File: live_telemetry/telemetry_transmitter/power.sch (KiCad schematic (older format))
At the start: 36 parts, among them J2 Battery In, J3 BUS_CONN, Q1 Q_NMOS_GSD, Q2 Q_NMOS_GSD, Q3 Q_PMOS_GSD, Q4 Q_PMOS_GSD, Q5 Q_NMOS_GSD, U3 AP2114H-3.3, U5 INA180, U6 AP1509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

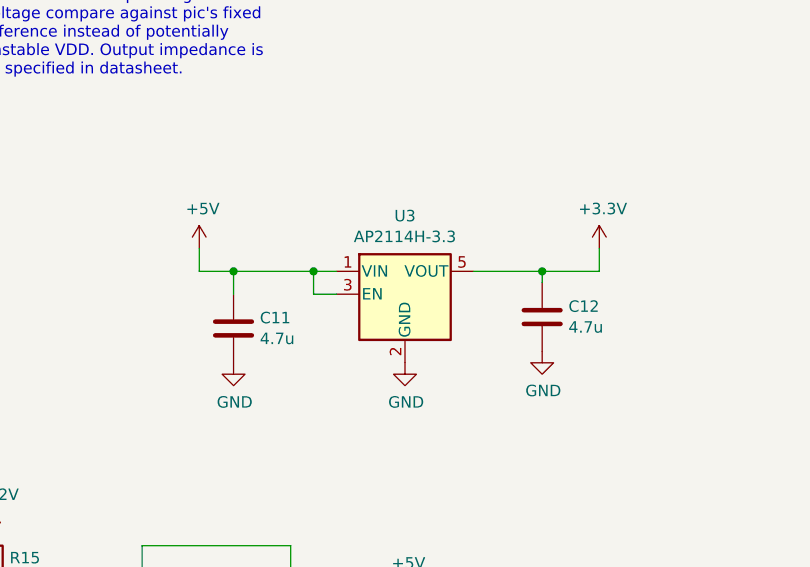
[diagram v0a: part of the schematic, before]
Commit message: Remove old/replaced components for LTT and LTR
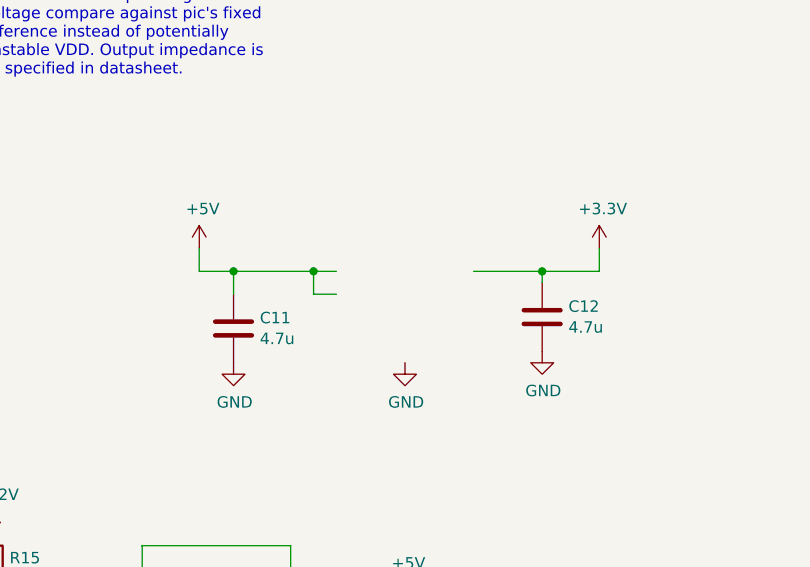
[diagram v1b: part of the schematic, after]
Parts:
- removed U3: AP2114H-3.3, Package_TO_SOT_SMD:SOT-23-5_HandSoldering, symbol Regulator_Linear:AP2112K-3.3
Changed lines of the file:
@@
 EESchema Schematic File Version 4
-EELAYER 26 0
+LIBS:telemetry_transmitter-cache
+EELAYER 29 0
 EELAYER END
 $Descr A4 11693 8268
@@
 	5000 1050 5000 1100
 $Comp
-L Regulator_Linear:AP2112K-3.3 U3
-U 1 1 5B9DEFF0
-P 9150 2600
-F 0 "U3" H 9150 2942 50  0000 C CNN
-F 1 "AP2114H-3.3" H 9150 2851 50  0000 C CNN
-F 2 "Package_TO_SOT_SMD:SOT-23-5_HandSoldering" H 9150 2925 50  0001 C CNN
-F 3 "https://www.diodes.com/assets/Datasheets/AP2112.pdf" H 9150 2700 50  0001 C CNN
-	1    9150 2600
-	1    0    0    -1
-$EndComp
-$Comp
 L Device:D_Zener D4

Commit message: Add placeholder LDOs for LTT and LTR
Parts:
- added U?: ?, Package_TO_SOT_SMD:TSOT-23-5, symbol Regulator_Linear:NCV8114ASN330T1G
- C11, C12: value 4.7u -> 1uF
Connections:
- wire segments 111 -> 112
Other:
- note added: "5V to 3.3V VOLTAGE REGULATOR"
- note added: "Note: The actual voltage regulator part # has not been selected yet. TBD ASAP."
- moved on the sheet: C11
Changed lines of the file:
@@
 L Device:C C11
 U 1 1 5B9E51A5
-P 8400 2750
-F 0 "C11" H 8285 2704 50  0000 R CNN
-F 1 "4.7u" H 8285 2795 50  0000 R CNN
-F 2 "Capacitor_SMD:C_0805_2012Metric_Pad1.15x1.40mm_HandSolder" H 8438 2600 50  0001 C CNN
-F 3 "~" H 8400 2750 50  0001 C CNN
-	1    8400 2750
+P 8350 2750
+F 0 "C11" H 8235 2704 50  0000 R CNN
+F 1 "1uF" H 8235 2795 50  0000 R CNN
+F 2 "Capacitor_SMD:C_0805_2012Metric_Pad1.15x1.40mm_HandSolder" H 8388 2600 50  0001 C CNN
+F 3 "~" H 8350 2750 50  0001 C CNN
+	1    8350 2750
 	-1   0    0    1
 $EndComp
@@
 P 9750 2700
 F 0 "C12" H 9635 2654 50  0000 R CNN
-F 1 "4.7u" H 9635 2745 50  0000 R CNN
+F 1 "1uF" H 9635 2745 50  0000 R CNN
 F 2 "Capacitor_SMD:C_0805_2012Metric_Pad1.15x1.40mm_HandSolder" H 9788 2550 50  0001 C CNN
 F 3 "~" H 9750 2700 50  0001 C CNN
@@
 $EndComp
 Wire Wire Line
-	9450 2500 9750 2500
-Wire Wire Line
 	9750 2500 9750 2550
 Wire Wire Line
-	8400 2500 8400 2600
-Wire Wire Line
-	8850 2600 8750 2600
+	8350 2500 8350 2600
 $Comp
 L power:+5V #PWR042
@@
 L power:GND #PWR043
 U 1 1 5B9E6978
-P 8400 2900
-F 0 "#PWR043" H 8400 2650 50  0001 C CNN
-F 1 "GND" H 8405 2727 50  0000 C CNN
-F 2 "" H 8400 2900 50  0001 C CNN
-F 3 "" H 8400 2900 50  0001 C CNN
-	1    8400 2900
+P 8350 2900
+F 0 "#PWR043" H 8350 2650 50  0001 C CNN
+F 1 "GND" H 8355 2727 50  0000 C CNN
+F 2 "" H 8350 2900 50  0001 C CNN
+F 3 "" H 8350 2900 50  0001 C CNN
+	1    8350 2900
 	1    0    0    -1
 $EndComp
@@
 	10000 2400 10000 2500
 Wire Wire Line
-	8750 2600 8750 2500
-Wire Wire Line
-	8400 2500 8750 2500
-Connection ~ 8750 2500
-Wire Wire Line
-	8750 2500 8850 2500
-Wire Wire Line
 	8250 2400 8250 2500
 Wire Wire Line
-	8250 2500 8400 2500
-Connection ~ 8400 2500
+	8250 2500 8350 2500
 Text GLabel 9450 5100 0    50   Input ~ 0
 CANH
@@
 	1    0    0    -1
 $EndComp
+Wire Wire Line
+	9550 2500 9750 2500
+Wire Wire Line
+	9450 2500 9550 2500
+Connection ~ 9550 2500
+$Comp
+L Regulator_Linear:NCV8114ASN330T1G U?
+U 1 1 61536AE4
+P 9150 2600
+F 0 "U?" H 9150 2967 50  0000 C CNN
+F 1 "?" H 9150 2876 50  0000 C CNN
+F 2 "Package_TO_SOT_SMD:TSOT-23-5" H 9150 2200 50  0001 C CIN
+F 3 "https://ru.mouser.com/datasheet/2/308/NCV8114-D-1107616.pdf" H 9150 2100 50  0001 C CNN
+	1    9150 2600
+	1    0    0    -1
+$EndComp
+Wire Wire Line
+	8750 2700 8650 2700
+Wire Wire Line
+	8650 2700 8650 2500
+Connection ~ 8650 2500
+Wire Wire Line
+	8650 2500 8750 2500
+Connection ~ 8350 2500
+Wire Wire Line
+	8350 2500 8650 2500
+Wire Notes Line
+	8050 2150 8050 3300
+Wire Notes Line
+	8050 3300 10200 3300
+Wire Notes Line
+	10200 3300 10200 2150
+Wire Notes Line
+	10200 2150 8050 2150
+Text Notes 8550 3250 0    50   ~ 10
+5V to 3.3V VOLTAGE REGULATOR
+Text Notes 7700 2100 0    50   ~ 10
+Note: The actual voltage regulator part # has not been selected yet. TBD ASAP.
 $EndSCHEMATC

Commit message: Add back LTR power.sch with battery connection, label symbols
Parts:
- gave numbers to parts that had none: 1
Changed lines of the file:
@@
 Connection ~ 9550 2500
 $Comp
-L Regulator_Linear:NCV8114ASN330T1G U?
+L Regulator_Linear:NCV8114ASN330T1G U3
 U 1 1 61536AE4
 P 9150 2600
-F 0 "U?" H 9150 2967 50  0000 C CNN
+F 0 "U3" H 9150 2967 50  0000 C CNN
 F 1 "?" H 9150 2876 50  0000 C CNN
 F 2 "Package_TO_SOT_SMD:TSOT-23-5" H 9150 2200 50  0001 C CIN

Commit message: Address PR comments and add in missing part #'s
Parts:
- removed U3: ?, Package_TO_SOT_SMD:TSOT-23-5, symbol Regulator_Linear:NCV8114ASN330T1G
- added U?: TLV70233QDBVRQ1, symbol canhw:TLV70233QDBVRQ1
- D4: value Schottky Diode -> SD1206S040S2R0
- F1: value Fuse -> F4989-ND, 36-3557-2-ND
- R10: value R -> 5K
- R11: value R -> 20K
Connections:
- wire segments 112 -> 120
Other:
- note added: "0.2R with \n1/4 W rating"
- note added: "12V to 5V BUCK CONVERTER"
- note added: "BATT VSENSE VOLTAGE DIVIDER"
- note added: "BATTERY CONNECTOR AND CURRENT SENSING"
- note added: "BUS CURRENT SENSING"
- note added: "CAN BUS CONNECTOR"
- note added: "Overspec'd Fuse\nof 58 V, 10A\n(Fuse & Holder)"
- moved on the sheet: C10, C11, C12, C5, C6, C7, C8, C9, D4, F1, J2, J3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

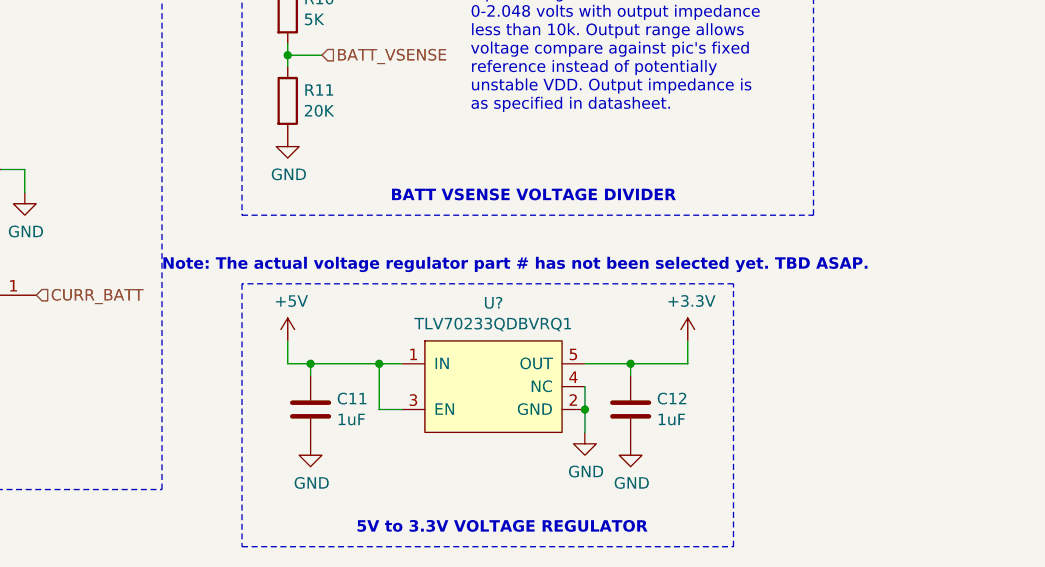
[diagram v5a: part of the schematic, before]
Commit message: Update radio schematics and set foot print associations
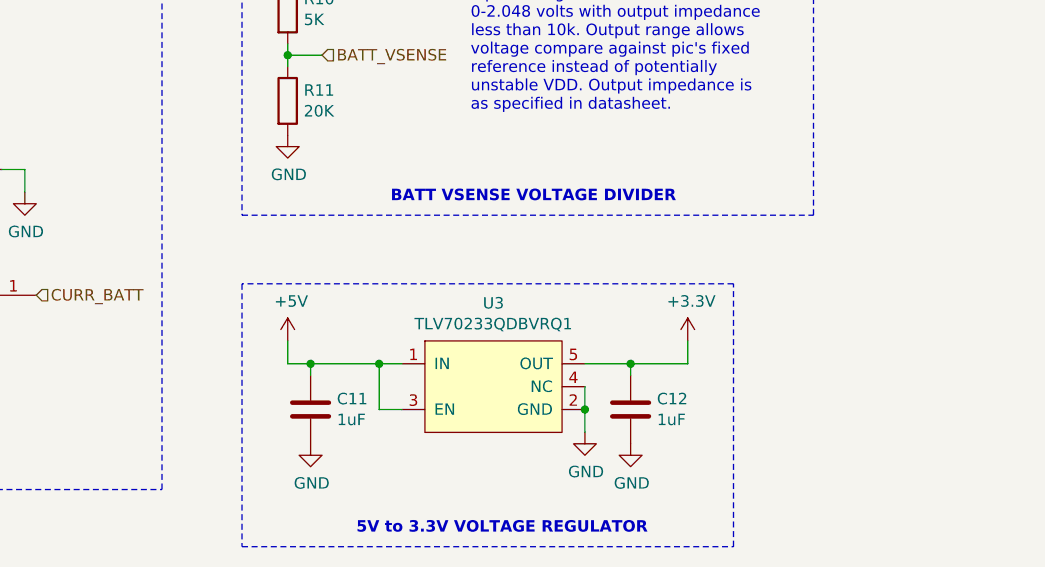
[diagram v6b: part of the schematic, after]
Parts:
- U3: renamed from U?; footprint (none) -> Package_TO_SOT_SMD:SOT-23-5_HandSoldering
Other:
- note removed: "Note: The actual voltage regulator part # has not been selected yet. TBD ASAP."
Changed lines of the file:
@@
 Text Notes 9000 3400 0    50   ~ 10
 5V to 3.3V VOLTAGE REGULATOR
-Text Notes 8150 2250 0    50   ~ 10
-Note: The actual voltage regulator part # has not been selected yet. TBD ASAP.
 Text Notes 6250 1100 0    50   ~ 0
 0.2R with \n1/4 W rating
@@
 	5800 1100 5800 1400
 $Comp
-L canhw:TLV70233QDBVRQ1 U?
+L canhw:TLV70233QDBVRQ1 U3
 U 1 1 615CA06D
 P 9600 3000
-F 0 "U?" H 9600 3615 50  0000 C CNN
+F 0 "U3" H 9600 3615 50  0000 C CNN
 F 1 "TLV70233QDBVRQ1" H 9600 3524 50  0000 C CNN
-F 2 "" H 9600 2950 50  0001 C CNN
+F 2 "Package_TO_SOT_SMD:SOT-23-5_HandSoldering" H 9600 2950 50  0001 C CNN
 F 3 "" H 9600 2950 50  0001 C CNN
 	1    9600 3000

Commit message: Update LTT first pass layout
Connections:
- net +12V: now also C5.1; no longer C5.2
- net +5V: now also C9.1; no longer C9.2
- net GND: now also C5.2, C9.2; no longer C5.1, C9.1
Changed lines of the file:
@@
-$EndComp
-$Comp
-L Device:C C9
-U 1 1 5B9E08AC
-P 3000 3250
-F 0 "C9" H 2885 3204 50  0000 R CNN
-F 1 "100u" H 2885 3295 50  0000 R CNN
-F 2 "Capacitor_THT:CP_Radial_D7.5mm_P2.50mm" H 3038 3100 50  0001 C CNN
-F 3 "~" H 3000 3250 50  0001 C CNN
-	1    3000 3250
-	-1   0    0    1
 $EndComp
 $Comp
@@
 	2250 3000 2500 3000
 Wire Wire Line
-	3000 3100 3000 3000
-Wire Wire Line
 	3000 3000 2800 3000
 $Comp
@@
 U 1 1 5BB56714
 P 2050 1350
-F 0 "C5" V 1900 1400 50  0000 R CNN
-F 1 "100u" V 1800 1450 50  0000 R CNN
+F 0 "C5" V 2200 1400 50  0000 R CNN
+F 1 "100u" V 2300 1450 50  0000 R CNN
 F 2 "Capacitor_THT:CP_Radial_D7.5mm_P2.50mm" H 2088 1200 50  0001 C CNN
 F 3 "~" H 2050 1350 50  0001 C CNN
 	1    2050 1350
-	0    -1   -1   0
+	0    1    1    0
 $EndComp
 Wire Wire Line
@@
 Wire Wire Line
 	2800 3500 3000 3500
-Wire Wire Line
-	3000 3500 3000 3400
 Connection ~ 2800 3500
 Wire Wire Line
@@
 Wire Wire Line
 	8800 2650 9100 2650
+Wire Wire Line
+	3000 3100 3000 3000
+Wire Wire Line
+	3000 3500 3000 3400
+$Comp
+L Device:C C9
+U 1 1 5B9E08AC
+P 3000 3250
+F 0 "C9" H 3200 3300 50  0000 R CNN
+F 1 "100u" H 3300 3200 50  0000 R CNN
+F 2 "Capacitor_THT:CP_Radial_D7.5mm_P2.50mm" H 3038 3100 50  0001 C CNN
+F 3 "~" H 3000 3250 50  0001 C CNN
+	1    3000 3250
+	1    0    0    -1
+$EndComp
 $EndSCHEMATC

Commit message: Address Jack's PR comments
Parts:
- added JP3: Jumper, Jumper:SolderJumper-2_P1.3mm_Open_RoundedPad1.0x1.5mm, symbol Device:Jumper
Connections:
- net +12V: now also JP3.1
- net at J3.1 (Pin_1), Q3.3 (D): now also JP3.2
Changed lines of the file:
@@
 Sheet 2 3
 Title "Live Telemetry Transmitter"
-Date "2021-10-01"
+Date "2021-11-03"
 Rev "2.1"
 Comp ""
@@
 	6950 4650 6950 4100
 Wire Wire Line
-	6950 4650 8400 4650
+	6950 4650 7600 4650
 Wire Notes Line
 	6900 6400 10100 6400
@@
 	1    0    0    -1
 $EndComp
+$Comp
+L Device:Jumper JP3
+U 1 1 6183E0F8
+P 7600 4100
+F 0 "JP3" V 7554 4227 50  0000 L CNN
+F 1 "Jumper" V 7645 4227 50  0000 L CNN
+F 2 "Jumper:SolderJumper-2_P1.3mm_Open_RoundedPad1.0x1.5mm" H 7600 4100 50  0001 C CNN
+F 3 "~" H 7600 4100 50  0001 C CNN
+	1    7600 4100
+	0    1    1    0
+$EndComp
+Wire Wire Line
+	7600 4400 7600 4650
+$Comp
+L power:+12V #PWR028
+U 1 1 6184BB09
+P 7600 3800
+F 0 "#PWR028" H 7600 3650 50  0001 C CNN
+F 1 "+12V" H 7615 3973 50  0000 C CNN
+F 2 "" H 7600 3800 50  0001 C CNN
+F 3 "" H 7600 3800 50  0001 C CNN
+	1    7600 3800
+	1    0    0    -1
+$EndComp
+Connection ~ 7600 4650
+Wire Wire Line
+	7600 4650 8400 4650
 $EndSCHEMATC
